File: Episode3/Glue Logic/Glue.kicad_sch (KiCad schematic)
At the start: 22 parts, among them SW2 Boot Speed, U10 ATF750CL, U7 ATF22V10C, U8 ATF750CL, U9 ATF750CL, X1 12MHz

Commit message: Exploited every last macrocells I could.
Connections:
- net EXP1 is gone; now on net ~{RD}: U7.18 (I/O)
- net EXP2 is gone; now on net ~{WR}: U7.17 (I/O)
- net A10: now also U7.10 (I); no longer U7.9 (I)
- net A11: now also U7.11 (I); no longer U7.10 (I)
- net A12: now also U7.13 (I/OE); no longer U7.11 (I)
- net A13: now also U7.14 (I/O); no longer U7.13 (I/OE)
- net A14: now also U7.15 (I/O); no longer U7.14 (I/O)
- net A15: now also U7.16 (I/O); no longer U7.15 (I/O)
- net A4: now also U7.4 (I); no longer U7.3 (I)
- net A5: now also U7.5 (I); no longer U7.4 (I)
- net A6: now also U7.6 (I); no longer U7.5 (I)
- net A7: now also U7.7 (I); no longer U7.6 (I)
- net A8: now also U7.8 (I); no longer U7.7 (I)
- net A9: now also U7.9 (I); no longer U7.8 (I)
- net R/~{W}: now also U7.3 (I)
- net ~{RD}: no longer U9.18 (I/O)
- net ~{WR}: no longer U9.17 (I/O)
- net EXP3: no longer names the net of U10.17 (I/O)
- net EXP3: no longer U7.16 (I/O)
- no-connect marks 7 -> 10

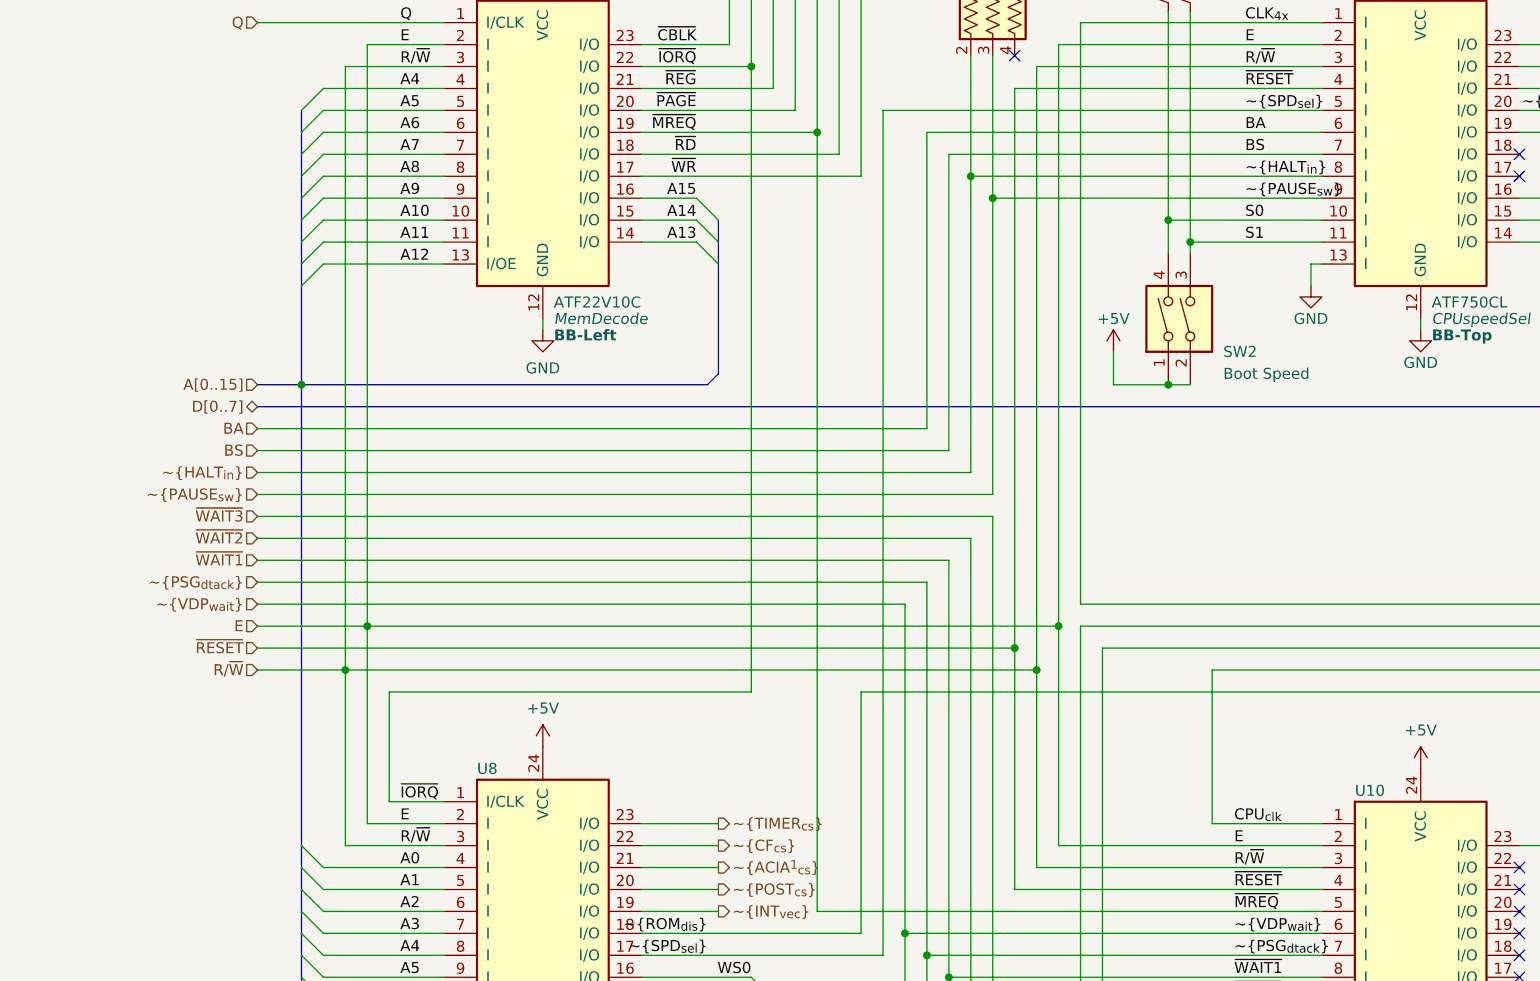
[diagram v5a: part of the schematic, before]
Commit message: Swapped E and IORQ pin on IOdecode
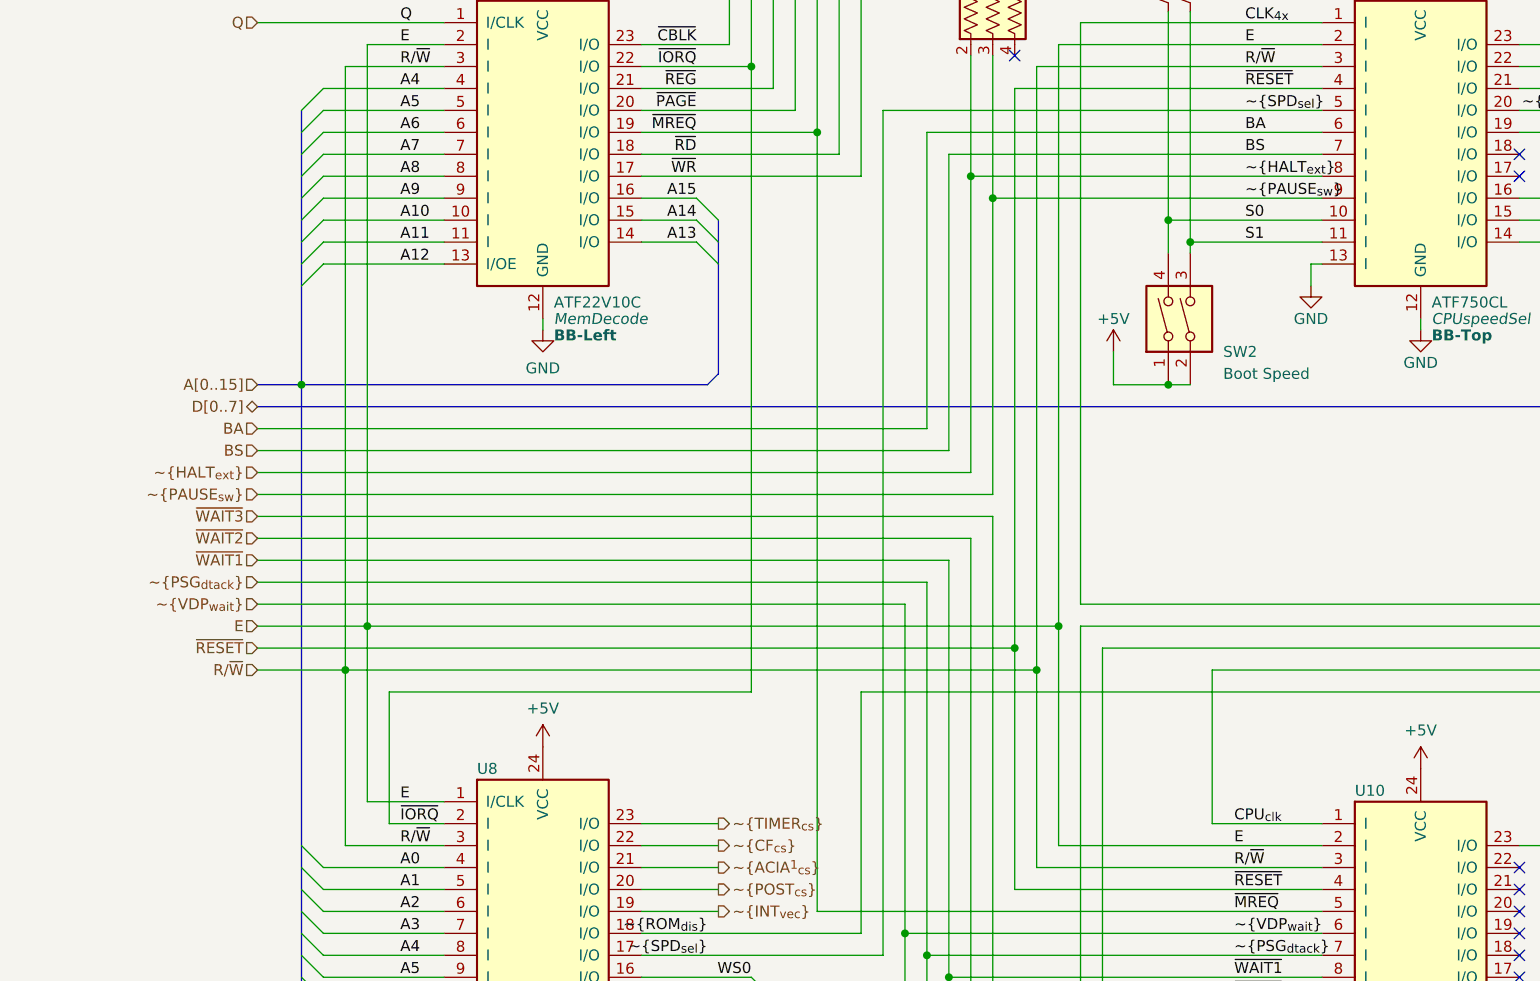
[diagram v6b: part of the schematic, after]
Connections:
- net E: now also U8.1 (I/CLK); no longer U8.2 (I)
- net ~{IORQ}: now also U8.2 (I); no longer U8.1 (I/CLK)
- net ~{HALT_{in}} renamed ~{HALT_{ext}}
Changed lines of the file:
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@@
 	(wire
 		(pts
+			(xy 53.34 119.38) (xy 53.34 134.62)
+		)
+		(stroke
+			(width 0)
+			(type default)
+		)
+	)
+	(wire
+		(pts
 			(xy 151.13 160.02) (xy 151.13 165.1)
 		)
@@
 	(wire
 		(pts
-			(xy 50.8 134.62) (xy 59.69 134.62)
-		)
-		(stroke
-			(width 0)
-			(type default)
-		)
-	)
-	(wire
-		(pts
 			(xy 146.05 40.64) (xy 146.05 67.31)
 		)
@@
 	(wire
 		(pts
+			(xy 53.34 134.62) (xy 59.69 134.62)
+		)
+		(stroke
+			(width 0)
+			(type default)
+		)
+	)
+	(wire
+		(pts
 			(xy 128.27 46.99) (xy 128.27 116.84)
 		)
@@
 	(wire
 		(pts
-			(xy 50.8 111.76) (xy 50.8 134.62)
+			(xy 50.8 111.76) (xy 50.8 132.08)
 		)
 		(stroke
@@
 	(wire
 		(pts
-			(xy 53.34 132.08) (xy 59.69 132.08)
+			(xy 50.8 132.08) (xy 59.69 132.08)
 		)
 		(stroke
@@
 	(wire
 		(pts
-			(xy 53.34 119.38) (xy 53.34 132.08)
-		)
-		(stroke
-			(width 0)
-			(type default)
-		)
-	)
-	(wire
-		(pts
 			(xy 148.59 134.62) (xy 161.29 134.62)
 		)
@@
 		)
 	)
-	(label "~{HALT_{in}}"
+	(label "~{HALT_{ext}}"
 		(at 152.4 59.69 0)
 		(effects
@@
 	)
 	(label "~{IORQ}"
-		(at 54.61 132.08 0)
+		(at 54.61 134.62 0)
 		(effects
 			(font
@@
 	)
 	(label "E"
-		(at 54.61 134.62 0)
+		(at 54.61 132.08 0)
 		(effects
 			(font
@@
 		)
 	)
-	(hierarchical_label "~{HALT_{in}}"
+	(hierarchical_label "~{HALT_{ext}}"
 		(shape input)
 		(at 38.1 93.98 180)
